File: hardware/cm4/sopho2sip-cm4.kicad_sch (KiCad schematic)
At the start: 0 parts

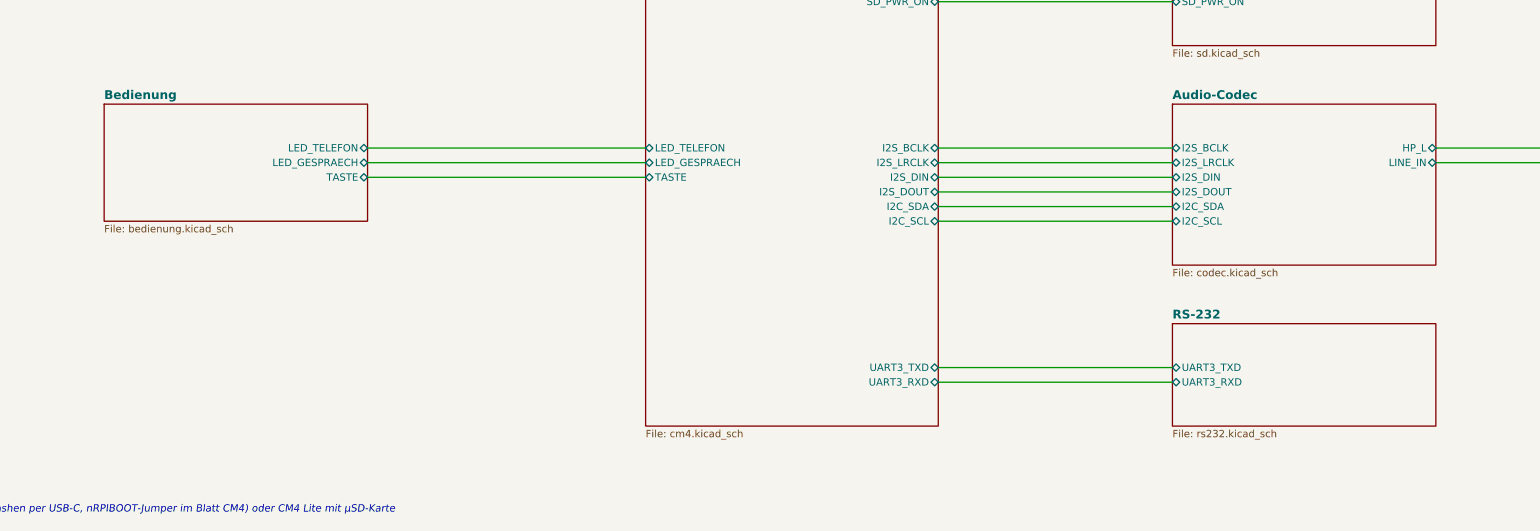
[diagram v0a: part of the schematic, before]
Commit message: CM4-Träger 0.3: Leiterplatte (4 Lagen, JLCPCB), Ein/Aus-Taster, Lüfter, lieferbare Teile
Schaltplan
- Codec TI TLV320AIC3204 statt WM8731 (abgekündigt); MCLK 12 MHz, Reset GPIO26, I²C an GPIO0/1
- Ein/Aus-Taster an GPIO3 (gpio-shutdown im Betrieb, Bootloader-Wecken im Halt)
- Lüfterblatt: AO3400A an GPIO12, Freilaufdiode, JST-PH-Anschluss; gpio-fan über SoC-Temperatur
- Konfig-Taster SW2 und Status-LED D3; Würth RJ45/RJ12, Bourns SM-LP-5001, TPD4E05U06
- reproduzierbare UUIDs (Schaltplan ↔ Platine bleiben verknüpft), eigene Footprints in hardware/bibliothek

Leiterplatte (erzeuge_layout.py)
- 110 × 85 mm, F.Cu / In1 GND / In2 +3V3 / B.Cu, JLC04161H-7628, JLCPCB-Regeln (.kicad_dru)
- CM4-Lage nach CM4IO-Referenz, Antennen-Sperrzone, isolierte Bereiche GND_ISO/GNDA mit Trennstreifen
- eigenes Fanout zu den Ebenen, Routing mit FreeRouting 1.9.0 über xvfb (2.x: Telemetrie an)
- DRC ohne Verstöße, 0 offene Verbindungen, Schaltplan ↔ Platine identisch
- Bestellliste für Digikey mit geprüftem Lagerbestand
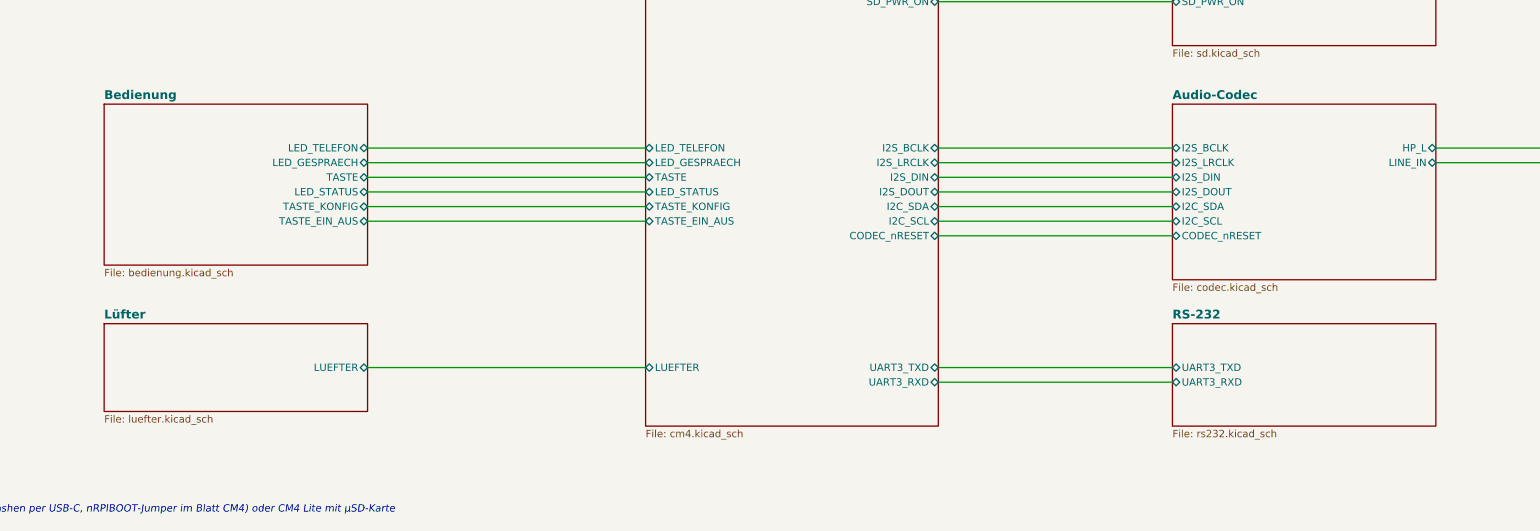
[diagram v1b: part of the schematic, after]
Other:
- added sheet Lüfter (luefter.kicad_sch)
- sheet Audio-Codec ports: added CODEC_nRESET; removed none
- sheet Bedienung ports: added LED_STATUS, TASTE_EIN_AUS, TASTE_KONFIG; removed none
- sheet CM4 ports: added CODEC_nRESET, LED_STATUS, LUEFTER, TASTE_EIN_AUS, TASTE_KONFIG; removed none
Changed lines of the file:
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@@
 	(wire (pts (xy 218.44 147.32) (xy 259.08 147.32)) (stroke (width 0) (type default)))
 	(wire (pts (xy 218.44 149.86) (xy 259.08 149.86)) (stroke (width 0) (type default)))
+	(wire (pts (xy 218.44 152.4) (xy 259.08 152.4)) (stroke (width 0) (type default)))
 	(wire (pts (xy 218.44 175.26) (xy 259.08 175.26)) (stroke (width 0) (type default)))
 	(wire (pts (xy 218.44 177.8) (xy 259.08 177.8)) (stroke (width 0) (type default)))
@@
 	(wire (pts (xy 119.38 139.7) (xy 167.64 139.7)) (stroke (width 0) (type default)))
 	(wire (pts (xy 119.38 142.24) (xy 167.64 142.24)) (stroke (width 0) (type default)))
+	(wire (pts (xy 119.38 144.78) (xy 167.64 144.78)) (stroke (width 0) (type default)))
+	(wire (pts (xy 119.38 147.32) (xy 167.64 147.32)) (stroke (width 0) (type default)))
+	(wire (pts (xy 119.38 149.86) (xy 167.64 149.86)) (stroke (width 0) (type default)))
+	(wire (pts (xy 119.38 175.26) (xy 167.64 175.26)) (stroke (width 0) (type default)))
 	(text "Speicher: CM4 mit eMMC (Flashen per USB-C, nRPIBOOT-Jumper im Blatt CM4) oder CM4 Lite mit µSD-Karte" (exclude_from_sim no) (at 30.16 200.66 0) (effects (font (size 1.27 1.27) italic) (justify left bottom)))
 	(text "Netz: WLAN/Bluetooth des CM4 (Antenne am Modul) oder Ethernet 10/100 (MagJack); beides gleichzeitig möglich" (exclude_from_sim no) (at 30.16 205.74 0) (effects (font (size 1.27 1.27) italic) (justify left bottom)))
@@
 		(pin "I2C_SDA" bidirectional (at 218.44 147.32 0) (effects (font (size 1.27 1.27)) (justify right)))
 		(pin "I2C_SCL" bidirectional (at 218.44 149.86 0) (effects (font (size 1.27 1.27)) (justify right)))
+		(pin "CODEC_nRESET" bidirectional (at 218.44 152.4 0) (effects (font (size 1.27 1.27)) (justify right)))
 		(pin "UART3_TXD" bidirectional (at 218.44 175.26 0) (effects (font (size 1.27 1.27)) (justify right)))
 		(pin "UART3_RXD" bidirectional (at 218.44 177.8 0) (effects (font (size 1.27 1.27)) (justify right)))
@@
 		(pin "LED_GESPRAECH" bidirectional (at 167.64 139.7 180) (effects (font (size 1.27 1.27)) (justify left)))
 		(pin "TASTE" bidirectional (at 167.64 142.24 180) (effects (font (size 1.27 1.27)) (justify left)))
+		(pin "LED_STATUS" bidirectional (at 167.64 144.78 180) (effects (font (size 1.27 1.27)) (justify left)))
+		(pin "TASTE_KONFIG" bidirectional (at 167.64 147.32 180) (effects (font (size 1.27 1.27)) (justify left)))
+		(pin "TASTE_EIN_AUS" bidirectional (at 167.64 149.86 180) (effects (font (size 1.27 1.27)) (justify left)))
+		(pin "LUEFTER" bidirectional (at 167.64 175.26 180) (effects (font (size 1.27 1.27)) (justify left)))
 		(instances
 			(project "sopho2sip-cm4"
-				(path "/4a9740d4-98df-4f49-9691-e6a39846794f" (page "2"))
+				(path "/c325dfb5-e80f-5288-9c1c-dd309ced8908" (page "2"))
 			)
 		)
@@
 		(instances
 			(project "sopho2sip-cm4"
-				(path "/4a9740d4-98df-4f49-9691-e6a39846794f" (page "3"))
+				(path "/c325dfb5-e80f-5288-9c1c-dd309ced8908" (page "3"))
 			)
 		)
@@
 		(instances
 			(project "sopho2sip-cm4"
-				(path "/4a9740d4-98df-4f49-9691-e6a39846794f" (page "4"))
+				(path "/c325dfb5-e80f-5288-9c1c-dd309ced8908" (page "4"))
 			)
 		)
 	)
-	(sheet (at 259.08 129.54) (size 45.72 27.94) (exclude_from_sim no) (in_bom yes) (on_board yes) (dnp no) (fields_autoplaced yes)
+	(sheet (at 259.08 129.54) (size 45.72 30.48) (exclude_from_sim no) (in_bom yes) (on_board yes) (dnp no) (fields_autoplaced yes)
 		(stroke (width 0.1524) (type solid))
 		(fill (color 0 0 0 0.0000))
 		(property "Sheetname" "Audio-Codec" (at 259.08 128.83 0) (effects (font (size 1.524 1.524) bold) (justify left bottom)))
-		(property "Sheetfile" "codec.kicad_sch" (at 259.08 158.08 0) (effects (font (size 1.27 1.27)) (justify left top)))
+		(property "Sheetfile" "codec.kicad_sch" (at 259.08 160.62 0) (effects (font (size 1.27 1.27)) (justify left top)))
 		(pin "I2S_BCLK" bidirectional (at 259.08 137.16 180) (effects (font (size 1.27 1.27)) (justify left)))
 		(pin "I2S_LRCLK" bidirectional (at 259.08 139.7 180) (effects (font (size 1.27 1.27)) (justify left)))
@@
 		(pin "I2C_SDA" bidirectional (at 259.08 147.32 180) (effects (font (size 1.27 1.27)) (justify left)))
 		(pin "I2C_SCL" bidirectional (at 259.08 149.86 180) (effects (font (size 1.27 1.27)) (justify left)))
+		(pin "CODEC_nRESET" bidirectional (at 259.08 152.4 180) (effects (font (size 1.27 1.27)) (justify left)))
 		(pin "HP_L" bidirectional (at 304.8 137.16 0) (effects (font (size 1.27 1.27)) (justify right)))
 		(pin "LINE_IN" bidirectional (at 304.8 139.7 0) (effects (font (size 1.27 1.27)) (justify right)))
 		(instances
 			(project "sopho2sip-cm4"
-				(path "/4a9740d4-98df-4f49-9691-e6a39846794f" (page "5"))
+				(path "/c325dfb5-e80f-5288-9c1c-dd309ced8908" (page "5"))
 			)
 		)
@@
 		(instances
 			(project "sopho2sip-cm4"
-				(path "/4a9740d4-98df-4f49-9691-e6a39846794f" (page "6"))
+				(path "/c325dfb5-e80f-5288-9c1c-dd309ced8908" (page "6"))
 			)
 		)
@@
 		(instances
 			(project "sopho2sip-cm4"
-				(path "/4a9740d4-98df-4f49-9691-e6a39846794f" (page "7"))
+				(path "/c325dfb5-e80f-5288-9c1c-dd309ced8908" (page "7"))
 			)
 		)
@@
 		(instances
 			(project "sopho2sip-cm4"
-				(path "/4a9740d4-98df-4f49-9691-e6a39846794f" (page "8"))
+				(path "/c325dfb5-e80f-5288-9c1c-dd309ced8908" (page "8"))
 			)
 		)
 	)
-	(sheet (at 73.66 129.54) (size 45.72 20.32) (exclude_from_sim no) (in_bom yes) (on_board yes) (dnp no) (fields_autoplaced yes)
+	(sheet (at 73.66 129.54) (size 45.72 27.94) (exclude_from_sim no) (in_bom yes) (on_board yes) (dnp no) (fields_autoplaced yes)
 		(stroke (width 0.1524) (type solid))
 		(fill (color 0 0 0 0.0000))
 		(property "Sheetname" "Bedienung" (at 73.66 128.83 0) (effects (font (size 1.524 1.524) bold) (justify left bottom)))
-		(property "Sheetfile" "bedienung.kicad_sch" (at 73.66 150.46 0) (effects (font (size 1.27 1.27)) (justify left top)))
+		(property "Sheetfile" "bedienung.kicad_sch" (at 73.66 158.08 0) (effects (font (size 1.27 1.27)) (justify left top)))
 		(pin "LED_TELEFON" bidirectional (at 119.38 137.16 0) (effects (font (size 1.27 1.27)) (justify right)))
 		(pin "LED_GESPRAECH" bidirectional (at 119.38 139.7 0) (effects (font (size 1.27 1.27)) (justify right)))
 		(pin "TASTE" bidirectional (at 119.38 142.24 0) (effects (font (size 1.27 1.27)) (justify right)))
+		(pin "LED_STATUS" bidirectional (at 119.38 144.78 0) (effects (font (size 1.27 1.27)) (justify right)))
+		(pin "TASTE_KONFIG" bidirectional (at 119.38 147.32 0) (effects (font (size 1.27 1.27)) (justify right)))
+		(pin "TASTE_EIN_AUS" bidirectional (at 119.38 149.86 0) (effects (font (size 1.27 1.27)) (justify right)))
 		(instances
 			(project "sopho2sip-cm4"
-				(path "/4a9740d4-98df-4f49-9691-e6a39846794f" (page "9"))
+				(path "/c325dfb5-e80f-5288-9c1c-dd309ced8908" (page "9"))
 			)
 		)
+	)
+	(sheet (at 73.66 167.64) (size 45.72 15.24) (exclude_from_sim no) (in_bom yes) (on_board yes) (dnp no) (fields_autoplaced yes)
+		(stroke (width 0.1524) (type solid))
+		(fill (color 0 0 0 0.0000))
+		(property "Sheetname" "Lüfter" (at 73.66 166.93 0) (effects (font (size 1.524 1.524) bold) (justify left bottom)))
+		(property "Sheetfile" "luefter.kicad_sch" (at 73.66 183.48 0) (effects (font (size 1.27 1.27)) (justify left top)))
+		(pin "LUEFTER" bidirectional (at 119.38 175.26 0) (effects (font (size 1.27 1.27)) (justify right)))
+		(instances
+			(project "sopho2sip-cm4"
+				(path "/c325dfb5-e80f-5288-9c1c-dd309ced8908" (page "10"))
+			)
+		)

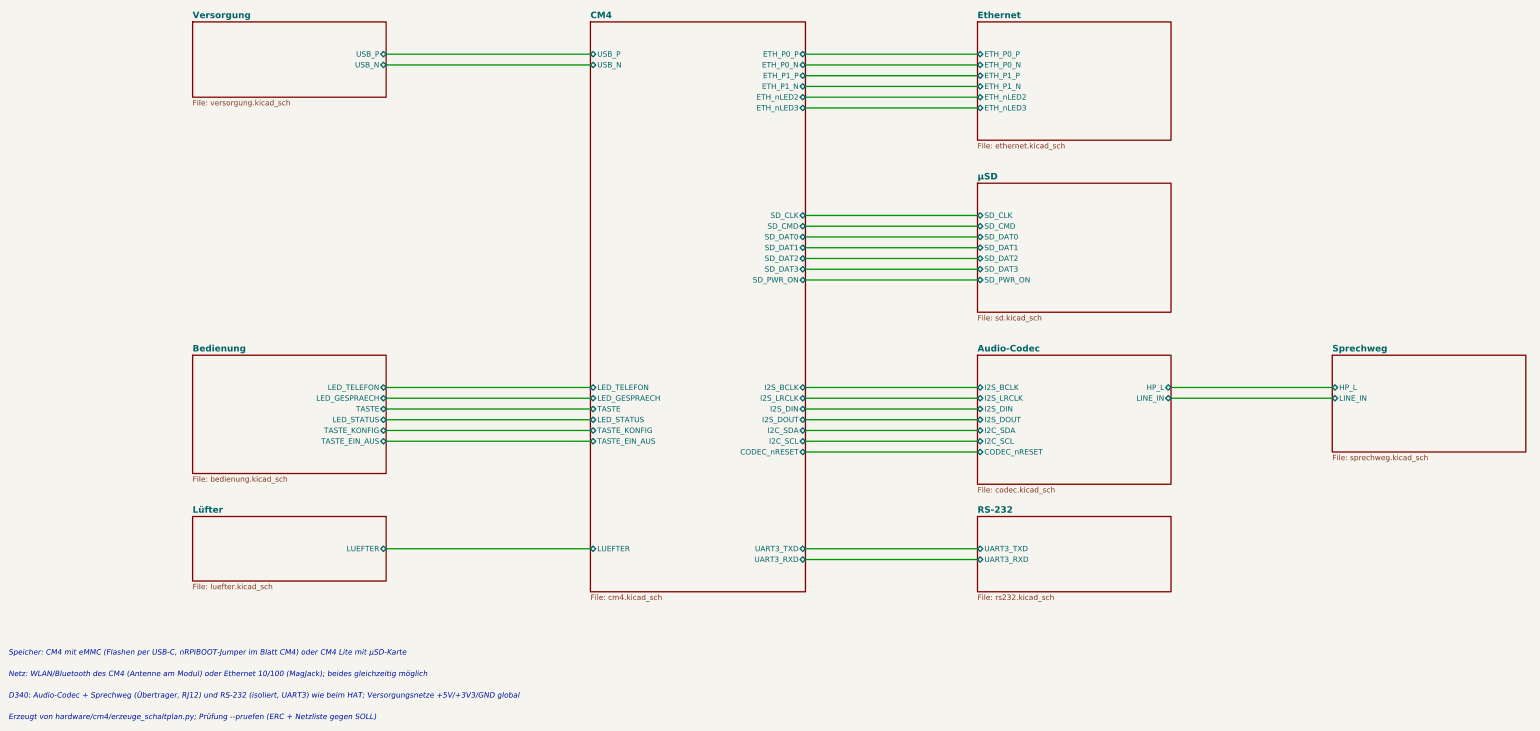
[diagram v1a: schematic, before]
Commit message: Schaltplan: Hinweise als Textkästen (KiCad bricht um); Texte werden in den Generator zurückgeführt
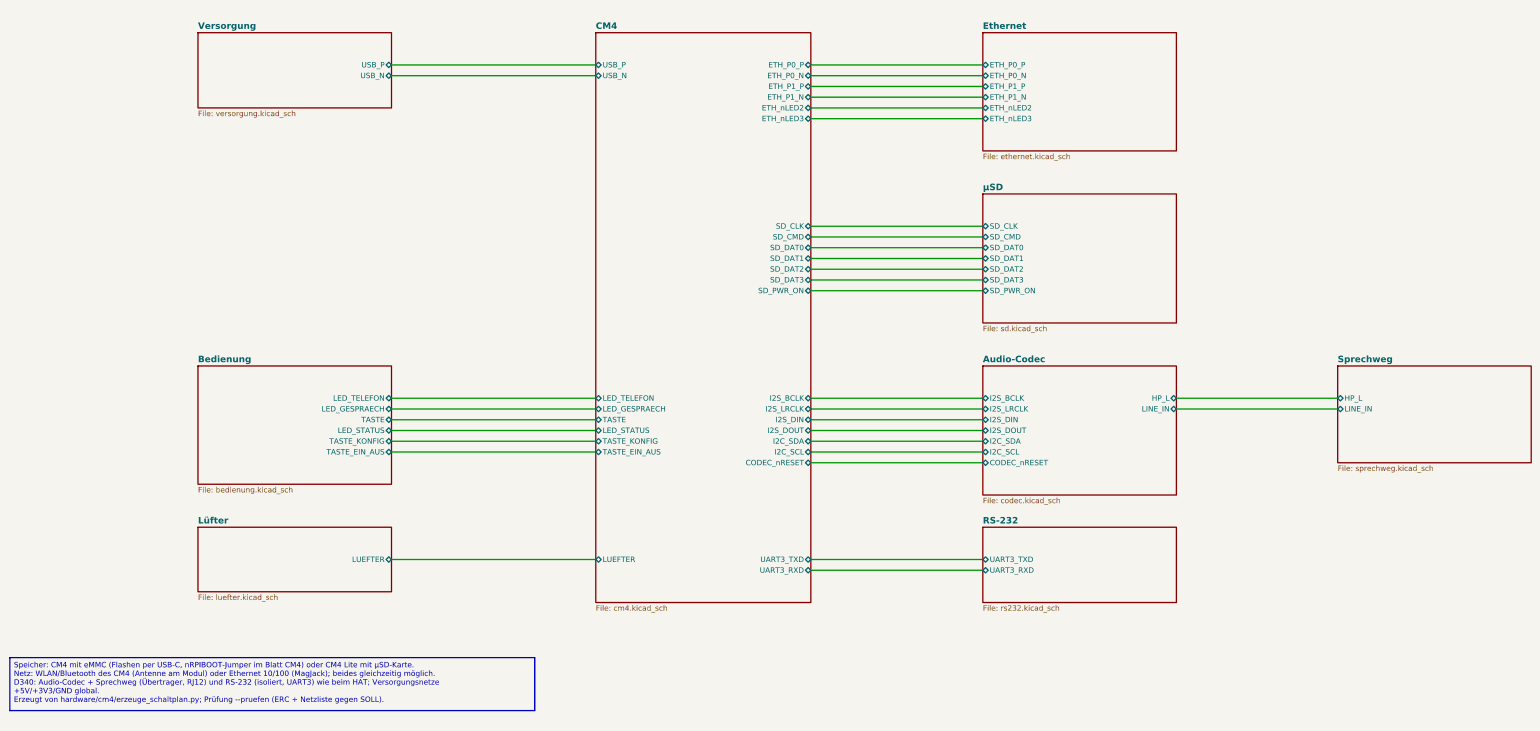
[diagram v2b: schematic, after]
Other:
- note removed: "D340: Audio-Codec + Sprechweg (Übertrager, RJ12) und RS-232 (isoliert, UART3) wie beim HAT; Versorgungsnetze +5V/+3V3/GND global"
- note removed: "Erzeugt von hardware/cm4/erzeuge_schaltplan.py; Prüfung --pruefen (ERC + Netzliste gegen SOLL)"
- note removed: "Netz: WLAN/Bluetooth des CM4 (Antenne am Modul) oder Ethernet 10/100 (MagJack); beides gleichzeitig möglich"
- note removed: "Speicher: CM4 mit eMMC (Flashen per USB-C, nRPIBOOT-Jumper im Blatt CM4) oder CM4 Lite mit µSD-Karte"
